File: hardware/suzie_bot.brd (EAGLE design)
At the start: 98.7 x 71.1 mm, 24 parts, among them IC1 LT1529CT33, IC2 L9637DDIP-ADAPTED, Y1 14.7456, Y2 6.0

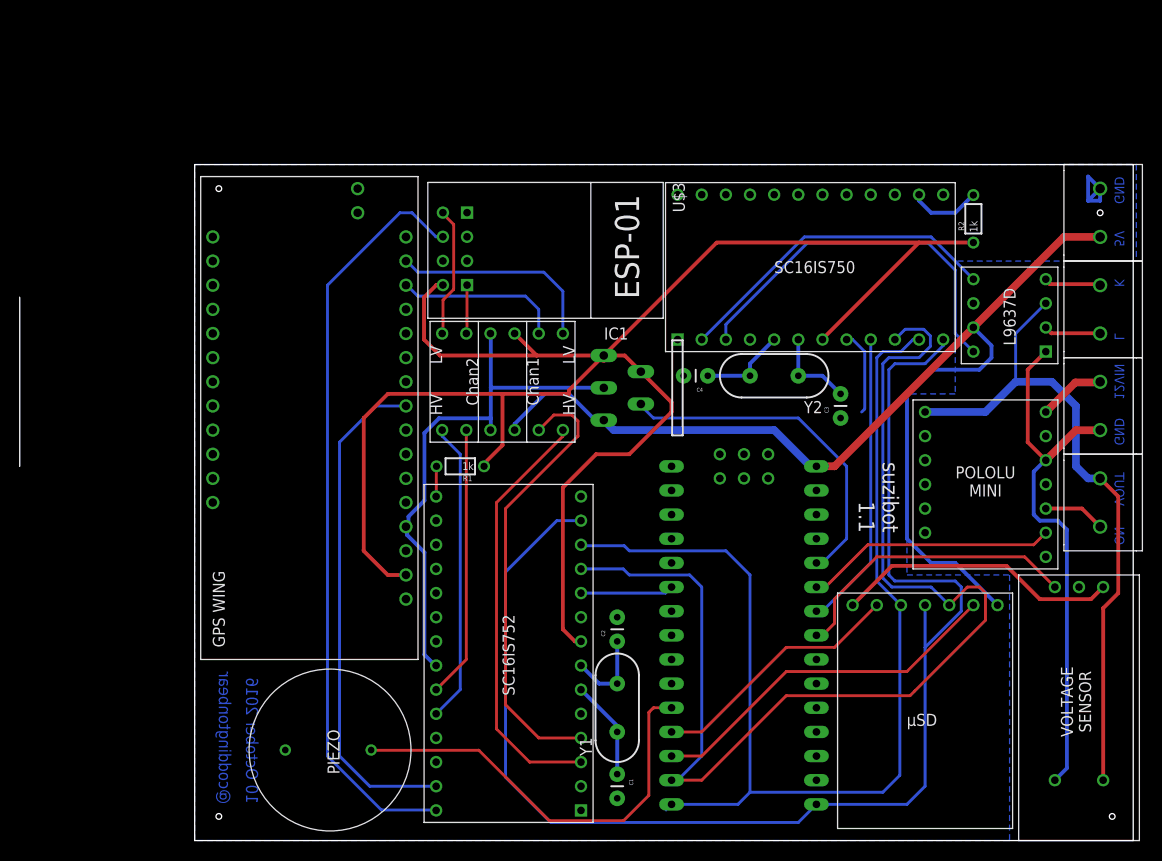
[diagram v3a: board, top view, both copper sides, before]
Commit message: SMD-ized;  pre-autorouting.
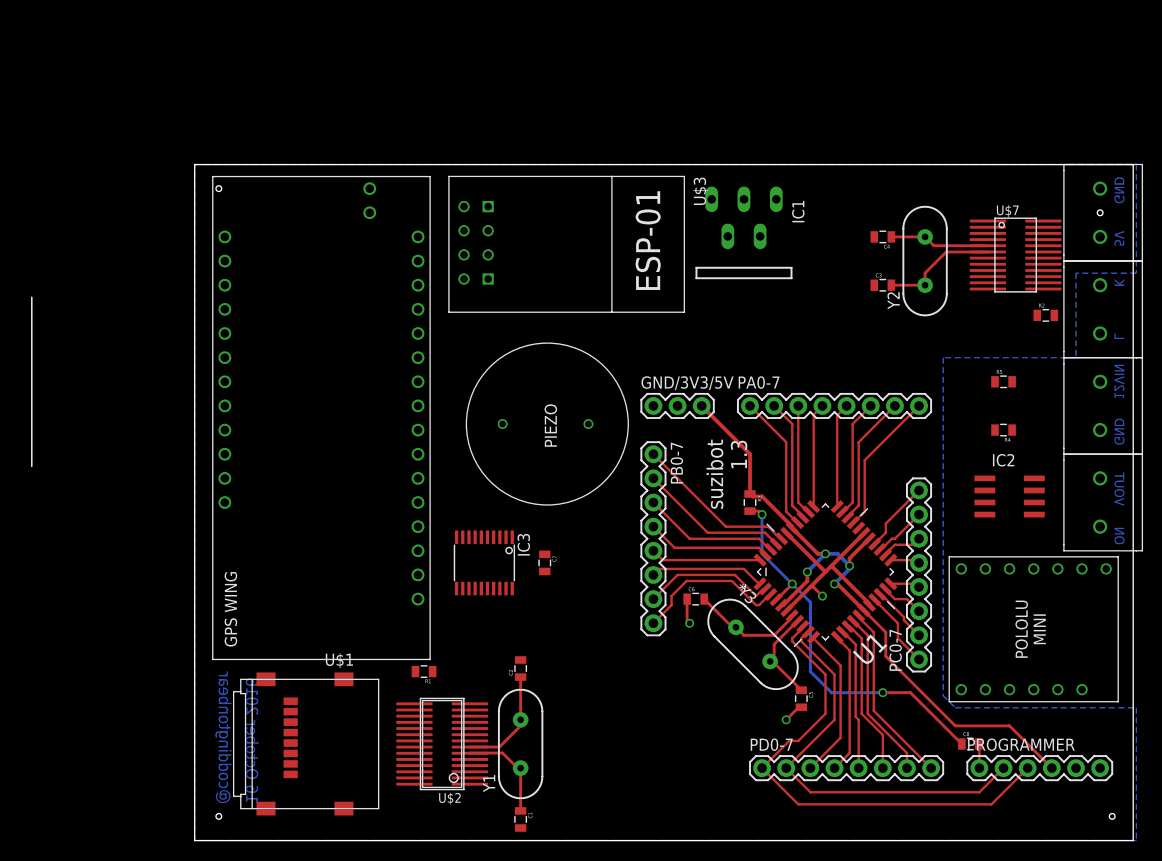
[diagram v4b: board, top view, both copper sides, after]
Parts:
- removed U$10: VOLTAGE-SENSOR, voltage-sensor:VOLTAGE-SENSOR
- removed U$6: LOGIC_LEVEL_CONVERTER, SparkFun-Boards:LOGIC_LEVEL_CONVERTER
- removed U$9: (no value), User-Submitted:LEVEL-SHIFTING-MICROSD
- added C5, C6: 22pF, SparkFun-Passives:0805
- added C7, C8: 0.1uF, SparkFun-Passives:0805
- added GND/3V3/5V: (no value), SparkFun-Connectors:1X03
- added IC3: IC_TXB0108-TSSOP-20, dp_devices.v6:TSSOP-20
- added PA0-7, PB0-7, PC0-7, PD0-7: (no value), SparkFun-Connectors:1X08_ROUND
- added PROGRAMMER: (no value), SparkFun-Connectors:1X06
- added R3: 10k, SparkFun-Passives:0805
- added R4: 70k, SparkFun-Passives:0805
- added R5: 50k, SparkFun-Passives:0805
- added U1: ATMEGA1284P-AU, Atmel_By_element14_Batch_1-00:QFP80P1200X1200X120-44N
- added Y3: 16.0, SparkFun-FreqCtrl:HC49US
- C1, C2, C3, C4: device SparkFun-Passives:CAP-PTH-SMALL -> SparkFun-Passives:0805
- IC2: value L9637DDIP-ADAPTED -> L9637D; device st-microelectronics:SO8-DIP-ADAPTER -> st-microelectronics:SO08
- R1, R2: device SparkFun-Passives:1/6W-RES -> SparkFun-Passives:0805
- U$1: value NANO -> CON_MICROSDHINGED; device Arduino-clone:NANO -> dp_devices.v6:CON_MICROSD_HINGED
- U$2: device nxp-semiconductors:TSSOP-28-ADAPTED -> nxp-semiconductors:TSSOP28
- U$7: value SC16IS750IPWDIP-24 -> SC16IS750IPW; device nxp-semiconductors:TSSOP-24-ADAPTED -> nxp-semiconductors:TSSOP-24
- moved U$1 47.1 mm to (12.7, 10.2), turned to 90 degrees
- moved U$11 41.2 mm to (38.1, 43.8)
- moved C4 23.5 mm to (72.4, 63.5)
- moved R1 21.9 mm to (24.1, 17.8)
- moved U$7 20.4 mm to (86.4, 61.6), turned to 270 degrees
- moved Y2 19.9 mm to (76.8, 61.0), turned to 90 degrees
- moved IC2 17.8 mm to (85.7, 36.2), turned to 270 degrees
- moved C3 14.7 mm to (72.4, 58.4), turned to 0 degrees
- moved U$4 14.5 mm to (88.3, 23.5), turned to 90 degrees
- moved IC1 13.1 mm to (57.8, 59.1), turned to 180 degrees
- moved R2 12.7 mm to (89.5, 55.2), turned to 0 degrees
- moved C1 11.2 mm to (34.3, 2.22)
- moved Y1 10.9 mm to (34.3, 10.2)
- moved C2 10.6 mm to (34.3, 18.1)
- moved U$2 10.0 mm to (26.0, 10.2), turned to 90 degrees
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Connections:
- removed net CS-GPSWIFI: U$1.D3, U$2.P$10
- removed net CS-KLINE: U$1.A5, U$7.P$9
- removed net CS-MICROSD: U$1.D10, U$9.CS
- removed net MISO: U$1.D12, U$2.P$12, U$7.P$11, U$9.DO
- removed net MOSI: U$1.D11, U$2.P$11, U$7.P$10, U$9.DI
- removed net N$30: U$1.A4, U$10.S
- removed net N$36: U$1.D8, U$11.P$2
- removed net SCLK: U$1.D13, U$2.P$13, U$7.P$12, U$9.SCK
- new net N$11: IC3.20, U$2.24
- new net N$12: IC3.11, U$2.23
- new net N$13: C8.1, R3.2, U1.4
- new net N$26: IC3.18, PB0-7.5, U1.44
- new net N$27: IC3.8, U$1.3
- new net N$28: IC3.9, U$1.7
- new net N$PD0/RXD0: PD0-7.1, PROGRAMMER.3, U1.9
- new net PA0: PA0-7.1, R4.2, R5.1, U1.37
- new net PA1: PA0-7.2, U1.36
- new net PA2: PA0-7.3, U1.35
- new net PA3: PA0-7.4, U1.34
- new net PA4: PA0-7.5, U1.33
- new net PA5: PA0-7.6, U1.32
- new net PA6: PA0-7.7, U1.31
- new net PA7: PA0-7.8, U1.30
- new net PB0: PB0-7.1, U$11.P$2, U1.40
- new net PB1: IC3.13, PB0-7.2, U1.41
- new net PB2: PB0-7.3, U1.42
- new net PB3: PB0-7.4, U$2.10, U1.43
- new net PB5/MOSI: IC3.17, PB0-7.6, U$2.11, U$7.10, U1.1
- new net PB6/MISO: IC3.16, PB0-7.7, U$2.12, U$7.11, U1.2
- new net PB7/SCLK: IC3.15, PB0-7.8, U$2.13, U$7.12, U1.3
- new net PC0: PC0-7.1, U1.19
- new net PC1: PC0-7.2, U1.20
- new net PC2: PC0-7.3, U1.21
- new net PC3: PC0-7.4, U1.22
- new net PC4: PC0-7.5, U1.23
- new net PC5: PC0-7.6, U1.24
- new net PC6: PC0-7.7, U1.25
- new net PC7: PC0-7.8, U$7.9, U1.26
- new net PD1/TXD0: PD0-7.2, PROGRAMMER.2, U1.10
- new net PD2/RXD1: PD0-7.3, U1.11
- new net PD3/TXD1: PD0-7.4, U1.12
- new net PD4: PD0-7.5, U1.13
- new net PD5: PD0-7.6, U1.14
- new net PD6: IC1.4, PD0-7.7, U1.15
- new net PD7: PD0-7.8, U$4.OFF, U1.16
- net 12V-OUT: now also IC2.7, R4.1; no longer IC2.VS, U$10.VCC
- net 3V3: now also GND/3V3/5V.2, IC3.3, U$1.4, U$2.8, U$7.7; no longer U$2.P$8, U$6.P$3, U$7.P$7
- net 5V: now also C7.1, GND/3V3/5V.3, IC2.3, IC3.1, PROGRAMMER.4, R3.1, U1.17, U1.27, U1.38, U1.5; no longer IC2.VCC, U$1.RAW, U$6.P$10, U$9.VCC
- net EXTGND: now also IC2.5, R5.2; no longer IC2.GND, U$10.GND
- net GND: now also C5.2, C6.1, C7.2, GND/3V3/5V.1, IC3.14, PROGRAMMER.5, PROGRAMMER.6, U$1.6, U$2.22, U$2.9, U$7.19, U$7.8, U1.18, U1.28, U1.39, U1.6; no longer U$1.GND, U$10.I, U$2.P$22, U$2.P$9, U$6.P$4, U$6.P$9, U$7.P$19, U$7.P$8, U$9.GND
- net K: now also IC2.6; no longer IC2.K
- net L: now also IC2.8; no longer IC2.LI
- net N$1: now also U$2.6; no longer U$2.P$6
- net N$10: now also C8.2, PROGRAMMER.1; no longer U$1.A6, U$4.OFF
- net N$14: now also IC3.6, U$5.RX-2; no longer U$5.TX-2, U$6.P$2
- net N$15: now also IC2.1, U$7.2; no longer IC2.RX, U$7.P$2
- net N$16: now also U$7.14; no longer U$7.P$14
- net N$17: now also IC3.10, U$2.4; no longer U$5.RX-2, U$6.P$1
- net N$18: now also U$2.15; no longer U$2.P$15
- net N$19: now also IC2.4, U$7.3; no longer IC2.TX, U$7.P$3
- net N$2: now also U$2.27; no longer U$2.P$27
- net N$20: now also U$7.5; no longer U$7.P$5
- net N$21: now also U$7.6; no longer U$7.P$6
- net N$22: now also IC3.5, U$5.TX-2; no longer U$2.P$23, U$6.P$8
- net N$23: now also IC3.19, U$2.3; no longer U$2.P$24, U$6.P$7
- net N$24: now also IC3.7, U$1.2; no longer U$2.P$3, U$6.P$12
- net N$25: now also IC3.12, U$1.5; no longer U$2.P$4, U$6.P$11
- net N$3: now also U$2.7; no longer U$2.P$7
- net N$4: now also U$2.28; no longer U$2.P$28
- net N$5: now also IC3.2; no longer U$6.P$6
- net N$6: now also C6.2, U1.7, Y3.1; no longer U$1.D9, U$9.CD
- net N$8: now also IC3.4; no longer U$6.P$5
- net N$9: now also C5.1, U1.8, Y3.2; no longer IC1.4, U$1.A7
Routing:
- net 3V3: track 186.8 -> 0.00 mm
- net SCLK: track 144.0 -> 0.00 mm
- net MOSI: track 125.7 -> 0.00 mm
- net MISO: track 118.8 -> 0.00 mm
- net N$4: track 79.7 -> 0.00 mm
- net GND: track 104.0 -> 29.5 mm, vias 0 -> 3
- net 12V-OUT: track 70.4 -> 0.00 mm
- net EXTGND: track 57.4 -> 0.00 mm
- net N$2: track 53.1 -> 0.00 mm
- net N$PD0/RXD0: track 0.00 -> 51.2 mm
- net 5V: track 119.6 -> 71.1 mm, vias 0 -> 4
- net N$25: track 47.9 -> 0.00 mm
- net N$36: track 44.7 -> 0.00 mm
- net N$24: track 44.7 -> 0.00 mm
- net PD1/TXD0: track 0.00 -> 43.2 mm
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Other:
- board text added: "16 October 2016"
- board text added: "suzibot 1.3"
- board text removed: "10 October 2016"
- board text removed: "suzibot 1.1"

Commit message: Fully layed-out.
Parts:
- moved C1 5.63 mm to (39.7, 3.81), turned to 0 degrees
- moved C2 5.63 mm to (39.7, 16.5), turned to 0 degrees
- moved U$1 5.08 mm to (7.62, 10.2), turned to 270 degrees
- moved IC3 4.02 mm to (31.8, 25.4), turned to 270 degrees
- moved R2 3.59 mm to (87.0, 52.7)
- moved C7 3.55 mm to (33.7, 30.8), turned to 180 degrees
- moved 5V/GND 2.54 mm to (95.2, 63.5)
- moved U$4 2.54 mm to (88.3, 21.0)
- moved GND/12V-IN 2.54 mm to (95.2, 43.2)
- moved K/L 2.54 mm to (95.2, 53.3)
- moved ON/12V-OUT 2.54 mm to (95.2, 33.0)
- moved Y1 2.54 mm to (36.8, 10.2)
- moved IC1 1.00 mm to (57.5, 58.1), turned to 0 degrees
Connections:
- removed net N$2: U$2.27, U$5.ENABLE
- removed net N$25: IC3.12, U$1.5
- removed net N$27: IC3.8, U$1.3
- removed net N$28: IC3.9, U$1.7
- removed net N$4: U$2.28, U$3.CH_PD
- new net MISO3V3: IC3.8, U$1.7, U$2.12
- new net MOSI3V3: IC3.7, U$1.3, U$2.11
- new net SKCK3V3: IC3.9, U$1.5, U$2.13
- net 12V-OUT: now also U$4.VOUT2
- net 3V3: now also IC3.2; no longer IC3.3
- net 5V: now also IC3.19, U1.29; no longer IC3.1
- net EXTGND: now also U$4.GND1, U$4.GND2, U$4.GND4
- net GND: now also IC3.11; no longer IC3.14
- net N$12: now also IC3.18; no longer IC3.11
- net N$14: now also IC3.5; no longer IC3.6
- net N$17: now also IC3.17; no longer IC3.10
- net N$22: now also IC3.4; no longer IC3.5
- net N$23: now also IC3.16; no longer IC3.19
- net N$24: now also IC3.6; no longer IC3.7
- net N$26: now also IC3.15; no longer IC3.18
- net N$5: now also IC3.1; no longer IC3.2
- net N$7: now also U$4.VIN2
- net N$8: now also IC3.3; no longer IC3.4
- net PA0: no longer R4.2, R5.1
- net PA5: now also IC1.4
- net PA6: now also U$3.CH_PD
- net PA7: now also R4.2, R5.1
- net PB1: now also IC3.10; no longer IC3.13
- net PB2: now also U$5.ENABLE
- net PB5/MOSI: now also IC3.14; no longer IC3.17, U$2.11
- net PB6/MISO: now also IC3.13; no longer IC3.16, U$2.12
- net PB7/SCLK: now also IC3.12; no longer IC3.15, U$2.13
- net PC6: now also U$4.OFF
- net PD6: no longer IC1.4
- net PD7: no longer U$4.OFF
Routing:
- net 3V3: track 0.00 -> 221.3 mm, vias 0 -> 2
- net 5V: track 71.1 -> 185.4 mm
- net PB5/MOSI: track 12.1 -> 84.5 mm, vias 0 -> 1
- net PB6/MISO: track 14.1 -> 86.4 mm, vias 0 -> 1
- net PB7/SCLK: track 16.3 -> 87.7 mm, vias 0 -> 1
- net N$8: track 0.00 -> 71.1 mm, vias 0 -> 2
- net N$5: track 0.00 -> 70.0 mm, vias 0 -> 2
- net N$12: track 0.00 -> 68.6 mm, vias 0 -> 4
- net N$14: track 0.00 -> 61.2 mm, vias 0 -> 2
- net N$23: track 0.00 -> 57.0 mm, vias 0 -> 2
- net EXTGND: track 0.00 -> 56.6 mm
- net PA6: track 13.8 -> 69.8 mm, vias 0 -> 2
- net N$22: track 0.00 -> 55.0 mm, vias 0 -> 2
- net N$17: track 0.00 -> 49.5 mm, vias 0 -> 2
- net N$19: track 0.00 -> 46.1 mm, vias 0 -> 4
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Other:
- board text added: "3V3"
- board text added: "CTS"
- board text added: "MISO"
- board text added: "MOSI"
- board text added: "PA"
- board text added: "PB"
- board text added: "PC"
- board text added: "PD"
- board text added: "PROG"
- board text added: "RST"
- board text added: "RX0"
- board text added: "RX1"
- board text added: "RXI"
- board text added: "SCK"
- board text added: "SCL"
- board text added: "SDA"
- board text added: "TX0"
- board text added: "TX1"
- board text added: "TXO"
- board text added: "VCC"
